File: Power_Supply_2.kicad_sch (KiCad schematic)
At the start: 8 parts

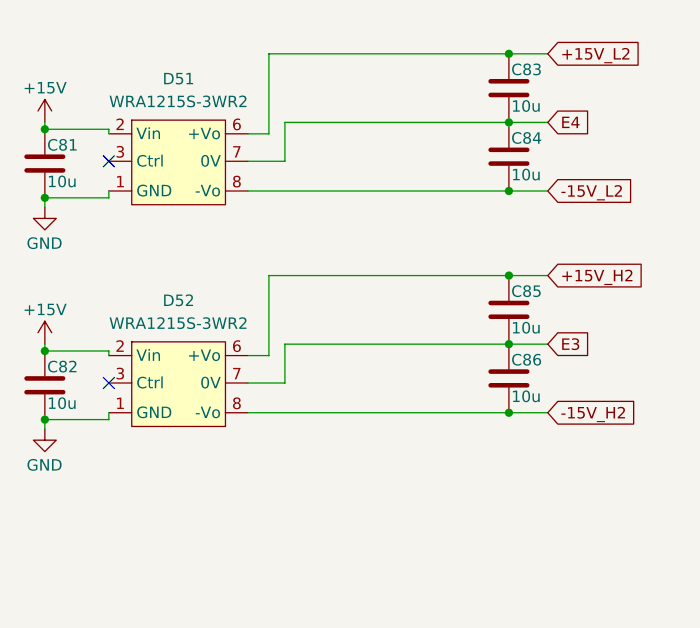
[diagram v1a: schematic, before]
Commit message: Изменил схему
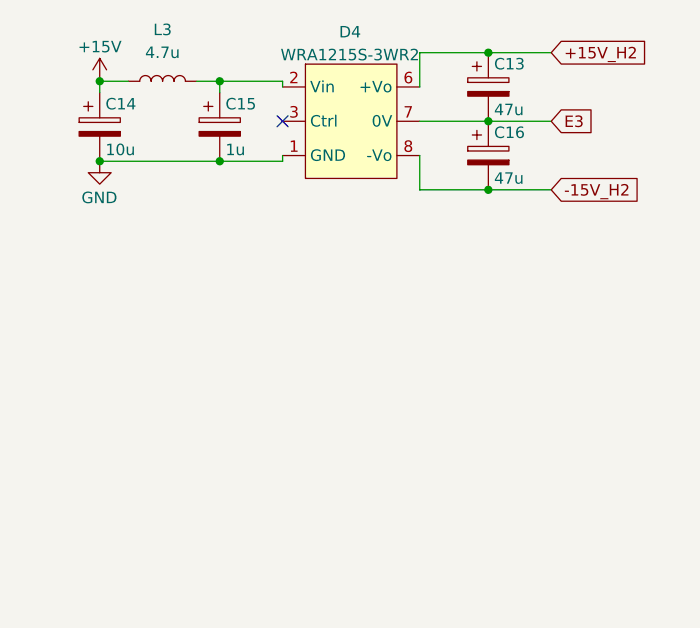
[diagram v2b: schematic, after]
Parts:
- removed C81, C82, C83, C84, C85, C86: 10u, Capacitor_SMD:C_1210_3225Metric_Pad1.33x2.70mm_HandSolder, symbol Device:C
- removed D51, D52: WRA1215S-3WR2, Mornsun:WRA1215S-3WR2, symbol Morsun:WRA1215S-3WR2
- added C13, C16: 47u, Capacitor_Tantalum_SMD:CP_EIA-7343-31_Kemet-D, symbol Device:C_Polarized
- added C14: 10u, Capacitor_Tantalum_SMD:CP_EIA-7343-31_Kemet-D, symbol Device:C_Polarized
- added C15: 1u, Capacitor_Tantalum_SMD:CP_EIA-3528-21_Kemet-B, symbol Device:C_Polarized
- added D4: WRA1215S-3WR2, Mornsun:WRA_S-3WR2, symbol Morsun:WRA1215S-3WR2
- added L3: 4.7u, Inductor_SMD:L_1812_4532Metric_Pad1.30x3.40mm_HandSolder, symbol Device:L
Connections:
- net +15V: now also C14.1, L3.1
- net +15V_H2: now also C13.1, D4.6 (+Vo)
- net -15V_H2: now also C16.2, D4.8 (-Vo)
- net E3: now also C13.2, C16.1, D4.7 (0V)
- net GND: now also C14.2, C15.2, D4.1 (GND)
- new net: C15.1, D4.2 (Vin), L3.2
- no-connect marks 2 -> 1

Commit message: Разместил все три стойки в своей области
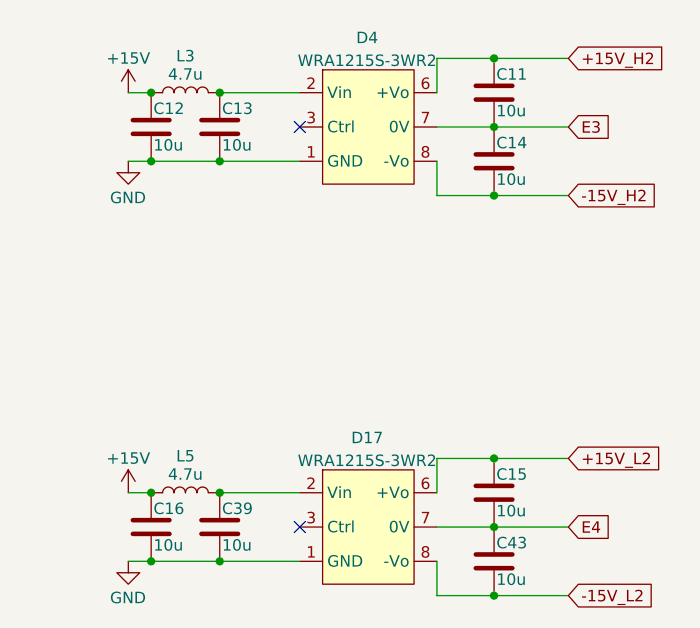
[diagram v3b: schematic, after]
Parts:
- removed C13, C16: 47u, Capacitor_Tantalum_SMD:CP_EIA-7343-31_Kemet-D, symbol Device:C_Polarized
- removed C14: 10u, Capacitor_Tantalum_SMD:CP_EIA-7343-31_Kemet-D, symbol Device:C_Polarized
- removed C15: 1u, Capacitor_Tantalum_SMD:CP_EIA-3528-21_Kemet-B, symbol Device:C_Polarized
- added C11, C12, C13, C14, C15, C16, C39, C43: 10u, Capacitor_SMD:C_1210_3225Metric_Pad1.33x2.70mm_HandSolder, symbol Device:C
- added D17: WRA1215S-3WR2, Mornsun:WRA_S-3WR2, symbol Morsun:WRA1215S-3WR2
- added L5: 4.7u, Inductor_SMD:L_1812_4532Metric_Pad1.30x3.40mm_HandSolder, symbol Device:L
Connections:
- net +15V: now also C12.1, C16.1, L5.1
- net +15V_H2: now also C11.1
- net -15V_H2: now also C14.2
- net E3: now also C11.2, C14.1
- net GND: now also C12.2, C13.2, C16.2, C39.2, D17.1 (GND)
- net at D4.2 (Vin), L3.2: now also C13.1
- new net: C39.1, D17.2 (Vin), L5.2
- new net +15V_L2: C15.1, D17.6 (+Vo)
- new net -15V_L2: C43.2, D17.8 (-Vo)
- new net E4: C15.2, C43.1, D17.7 (0V)
- no-connect marks 1 -> 2
